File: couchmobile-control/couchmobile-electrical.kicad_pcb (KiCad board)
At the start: 2 copper layers, 100 x 100 mm, 56 parts, among them J1 Power_In, J10 Motor1, J11 Motor2, J2 GPIO_NANO_1, J5 ESTOP_IRQ_EN, J6 BNO_COMM_CTRL, J7 Joystick, J8 Encoder1, J9 Encoder2, Q1 PMOS DGS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

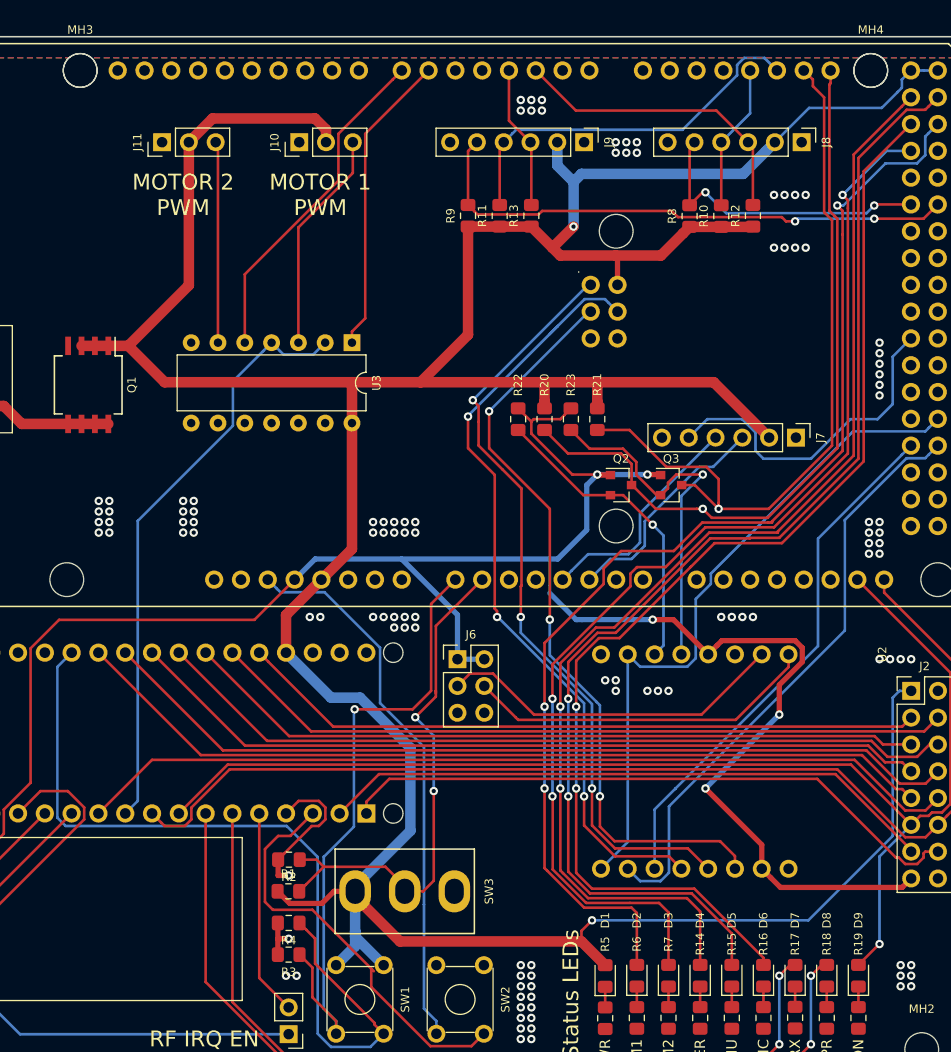
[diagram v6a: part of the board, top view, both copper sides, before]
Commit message: Changed some resistor values. Generated BOM.
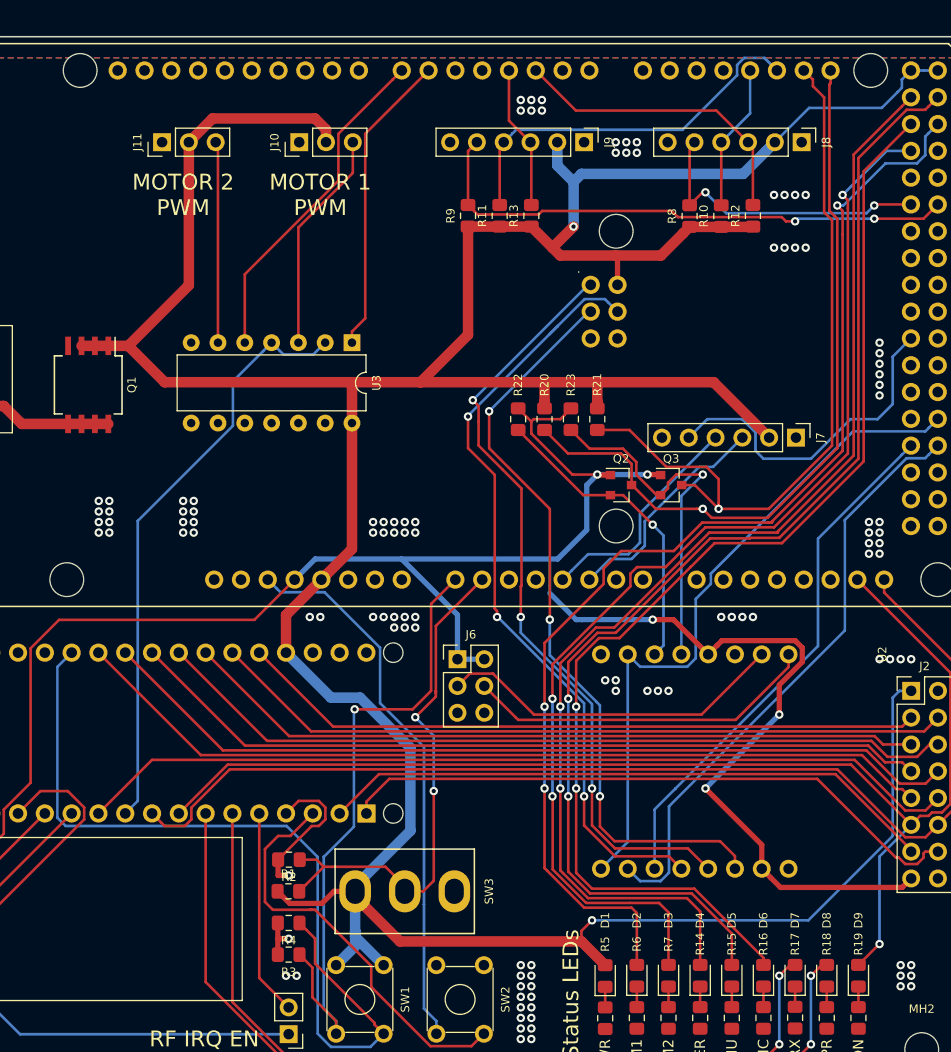
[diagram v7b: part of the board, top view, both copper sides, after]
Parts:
- removed MH3, MH4: MountingHole, MountingHole:MountingHole_3.2mm_M3_ISO7380
- Q2, Q3: value Q_NMOS_GSD -> BSS138
- R6, R7: value 10k -> 2.2k
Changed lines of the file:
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@@
     (thickness 1.6)
     (drawings 19)
-    (tracks 845)
+    (tracks 847)
     (zones 0)
-    (modules 56)
+    (modules 54)
     (nets 91)
   )
@@
     (pad 1 np_thru_hole circle (at 0 0) (size 3.2 3.2) (drill 3.2) (layers *.Cu *.Mask))
   )
-  (module MountingHole:MountingHole_3.2mm_M3_ISO7380 (layer F.Cu)
-    (at 35.24 23.2)
-    (descr "Mounting Hole 3.2mm, no annular, M3, ISO7380")
-    (tags "mounting hole 3.2mm no annular m3 iso7380")
-    (attr virtual)
-    (fp_text reference MH3 (at 0 -3.85) (layer F.SilkS)
-      (effects (font (size 0.8 0.8) (thickness 0.15)))
-    )
-    (fp_text value MountingHole (at 0 3.85) (layer F.Fab)
-      (effects (font (size 0.8 0.8) (thickness 0.15)))
-    )
-    (fp_text user %R (at 0.3 0) (layer F.Fab)
-      (effects (font (size 0.8 0.8) (thickness 0.15)))
-    )
-    (fp_circle (center 0 0) (end 2.85 0) (layer Cmts.User) (width 0.15))
-    (fp_circle (center 0 0) (end 3.1 0) (layer F.CrtYd) (width 0.05))
-    (pad 1 np_thru_hole circle (at 0 0) (size 3.2 3.2) (drill 3.2) (layers *.Cu *.Mask))
-  )
-  (module MountingHole:MountingHole_3.2mm_M3_ISO7380 (layer F.Cu)
-    (at 110.17 23.2)
-    (descr "Mounting Hole 3.2mm, no annular, M3, ISO7380")
-    (tags "mounting hole 3.2mm no annular m3 iso7380")
-    (attr virtual)
-    (fp_text reference MH4 (at 0 -3.85) (layer F.SilkS)
-      (effects (font (size 0.8 0.8) (thickness 0.15)))
-    )
-    (fp_text value MountingHole (at 0 3.85) (layer F.Fab)
-      (effects (font (size 0.8 0.8) (thickness 0.15)))
-    )
-    (fp_circle (center 0 0) (end 3.1 0) (layer F.CrtYd) (width 0.05))
-    (fp_circle (center 0 0) (end 2.85 0) (layer Cmts.User) (width 0.15))
-    (fp_text user %R (at 0.3 0) (layer F.Fab)
-      (effects (font (size 0.8 0.8) (thickness 0.15)))
-    )
-    (pad 1 np_thru_hole circle (at 0 0) (size 3.2 3.2) (drill 3.2) (layers *.Cu *.Mask))
-  )
   (module Resistor_SMD:R_0805_2012Metric_Pad1.15x1.40mm_HandSolder (layer F.Cu)
     (at 54.975 101)
@@
       (effects (font (size 0.8 0.8) (thickness 0.15)))
     )
-    (fp_text value 10k (at 0 1.65 270) (layer F.Fab)
+    (fp_text value 2.2k (at 0 1.65 270) (layer F.Fab)
       (effects (font (size 0.8 0.8) (thickness 0.15)))
     )
@@
       (effects (font (size 0.8 0.8) (thickness 0.15)))
     )
-    (fp_text value 10k (at 0 1.65 270) (layer F.Fab)
+    (fp_text value 2.2k (at 0 1.65 270) (layer F.Fab)
       (effects (font (size 0.8 0.8) (thickness 0.15)))
     )
@@
       (effects (font (size 0.8 0.8) (thickness 0.15)))
     )
-    (fp_text value Q_NMOS_GSD (at 0 2.5) (layer F.Fab)
+    (fp_text value BSS138 (at 0 2.5) (layer F.Fab)
       (effects (font (size 1 1) (thickness 0.15)))
     )
@@
       (effects (font (size 0.8 0.8) (thickness 0.15)))
     )
-    (fp_text value Q_NMOS_GSD (at 0 2.5) (layer F.Fab)
+    (fp_text value BSS138 (at 0 2.5) (layer F.Fab)
       (effects (font (size 1 1) (thickness 0.15)))
     )
@@
   (segment (start 57.75 97.75) (end 54.808601 94.808601) (width 0.25) (layer B.Cu) (net 72))
   (segment (start 54.808601 94.808601) (end 33.859471 94.808601) (width 0.25) (layer B.Cu) (net 72))
-  (segment (start 72.324999 115.675001) (end 68.435999 115.675001) (width 0.25) (layer F.Cu) (net 73))
-  (segment (start 73.5 114.5) (end 72.324999 115.675001) (width 0.25) (layer F.Cu) (net 73))
-  (segment (start 68.435999 115.675001) (end 62.824999 110.064001) (width 0.25) (layer F.Cu) (net 73))
-  (segment (start 62.824999 110.064001) (end 62.824999 108.324999) (width 0.25) (layer F.Cu) (net 73))
   (segment (start 55.16 95.75) (end 57.29 93.62) (width 0.25) (layer F.Cu) (net 73))
-  (segment (start 57.25 102.75) (end 53.5 102.75) (width 0.25) (layer F.Cu) (net 73))
-  (segment (start 63.074999 108.574999) (end 57.25 102.75) (width 0.25) (layer F.Cu) (net 73))
   (segment (start 52.75 102) (end 52.75 97) (width 0.25) (layer F.Cu) (net 73))
   (segment (start 52.75 97) (end 54 95.75) (width 0.25) (layer F.Cu) (net 73))
   (segment (start 53.5 102.75) (end 52.75 102) (width 0.25) (layer F.Cu) (net 73))
   (segment (start 54 95.75) (end 55.16 95.75) (width 0.25) (layer F.Cu) (net 73))
+  (segment (start 57.5 102.75) (end 57 102.75) (width 0.25) (layer F.Cu) (net 73))
+  (segment (start 62.824999 108.074999) (end 57.5 102.75) (width 0.25) (layer F.Cu) (net 73))
+  (segment (start 57 102.75) (end 53.5 102.75) (width 0.25) (layer F.Cu) (net 73))
+  (segment (start 57.25 102.75) (end 57 102.75) (width 0.25) (layer F.Cu) (net 73))
+  (segment (start 73.5 114.5) (end 72.324999 115.675001) (width 0.25) (layer F.Cu) (net 73))
+  (segment (start 72.324999 115.675001) (end 68.435999 115.675001) (width 0.25) (layer F.Cu) (net 73))
+  (segment (start 68.435999 115.675001) (end 62.824999 110.064001) (width 0.25) (layer F.Cu) (net 73))
+  (segment (start 62.824999 110.064001) (end 62.824999 108.074999) (width 0.25) (layer F.Cu) (net 73))
   (segment (start 67.82501 102.255943) (end 67.82501 87.32501) (width 0.25) (layer B.Cu) (net 74))
   (segment (start 67.824999 102.255954) (end 67.82501 102.255943) (width 0.25) (layer B.Cu) (net 74))
